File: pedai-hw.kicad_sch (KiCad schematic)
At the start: 31 parts, among them IC1 CD4051BQPWRQ1, IC2 CD4051BQPWRQ1, IC3 CD4051BQPWRQ1, J1 Conn_01x03, J10 Conn_01x01, J11 Conn_01x01, J12 Conn_01x01, J13 Conn_01x01, J14 Conn_01x01, J15 Conn_01x01, J16 left_connector_blackpill, J17 right_connector_blackpill, J18 Conn_01x01, J19 Conn_01x01, J2 Conn_01x01, J20 Conn_01x01, J21 Conn_01x01, J22 Conn_01x01, J23 Conn_01x01, J24 Conn_01x01, J25 Conn_01x01, J26 Conn_01x01, J27 Conn_01x01, J28 Conn_01x01, J3 Conn_01x01, J4 Conn_01x01, J5 Conn_01x01, J6 Conn_01x01, J7 Conn_01x01, J8 Conn_01x01, J9 Conn_01x01

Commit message: board is almost ready for production still looking for mistakes and inaccuracies
Signed-off-by: gmazzucchi <giacomo.mazzucchi@protonmail.com>
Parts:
- added H1, H2: MountingHole, MountingHole:MountingHole_4.3mm_M4, symbol Mechanical:MountingHole
- added J29: Conn_01x01, Connector_Wire:SolderWirePad_1x01_SMD_5x10mm, symbol Connector_Generic:Conn_01x01
- added R1, R2, R3: 1000, Resistor_SMD:R_1206_3216Metric, symbol Device:R
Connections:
- net +3.3V: now also J16.20 (Pin_20), R1.1, R2.1, R3.1; no longer J16.18 (Pin_18)
- net GND: now also J29.1 (Pin_1); no longer J17.2 (Pin_2)
- net MUX_D1: now also R1.2
- net MUX_D2: now also R2.2
- net MUX_D3: now also R3.2
- no-connect marks 27 -> 28
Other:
- note added: "Pull up resistors"

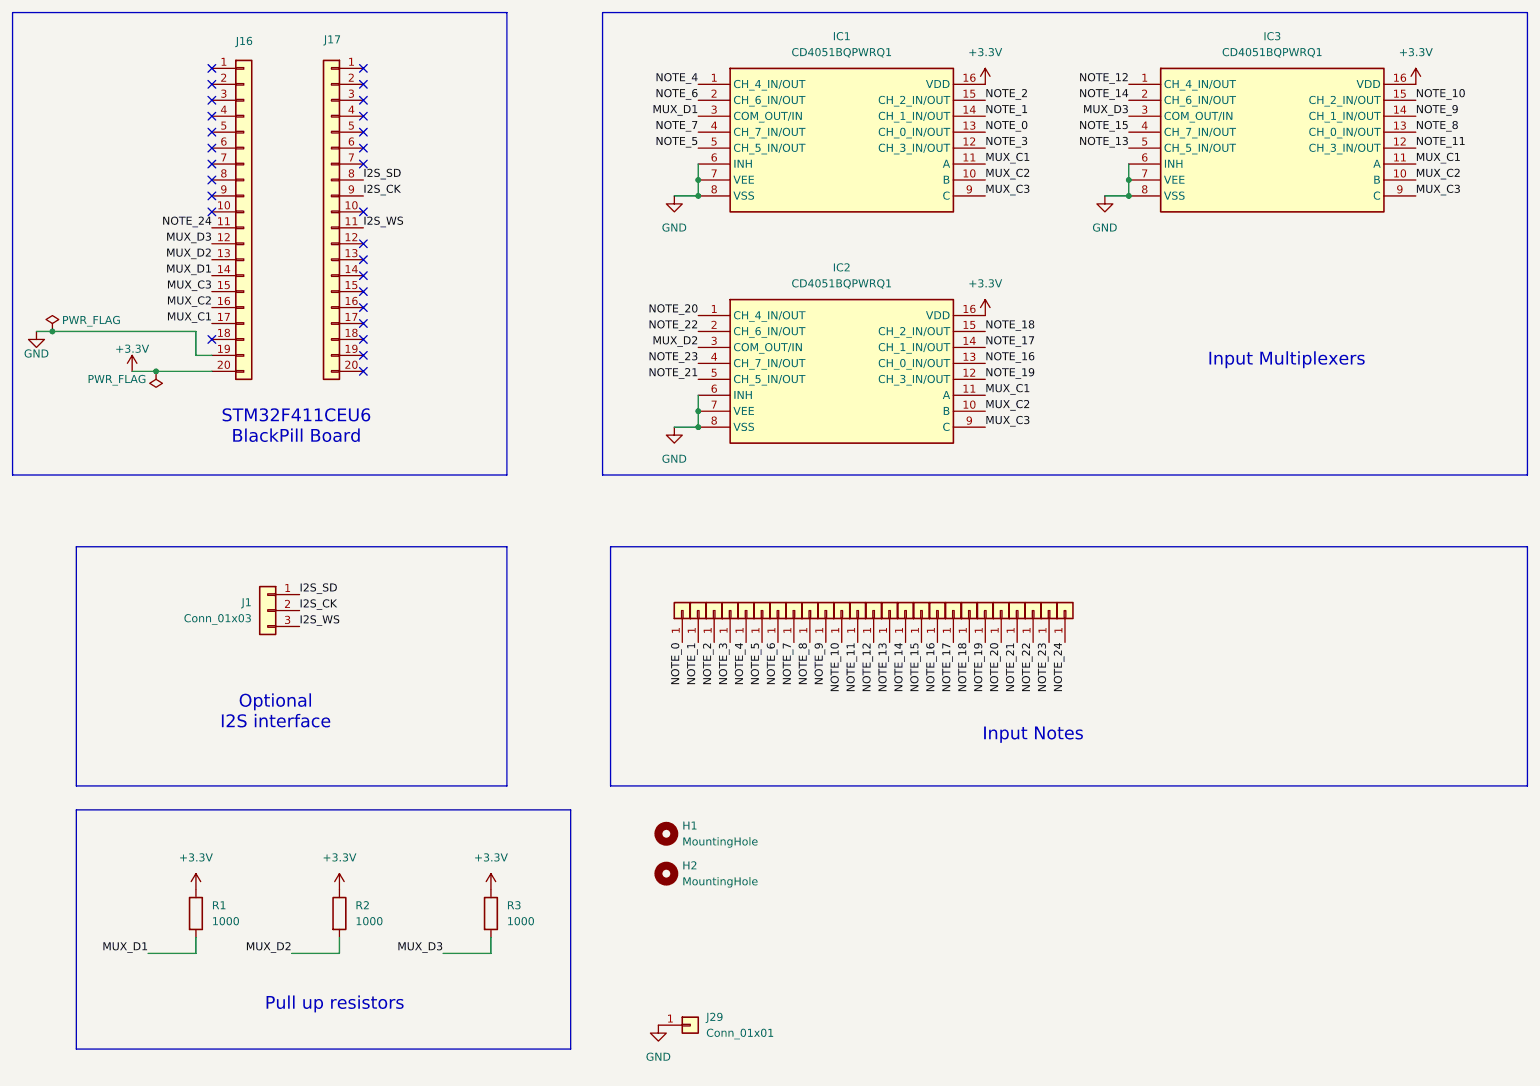
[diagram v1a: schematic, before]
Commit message: fix: removed multiplexer and attached directly to GPIOs fix: removed I2S interface for sound feat: added a UART to communicate with the mainboard
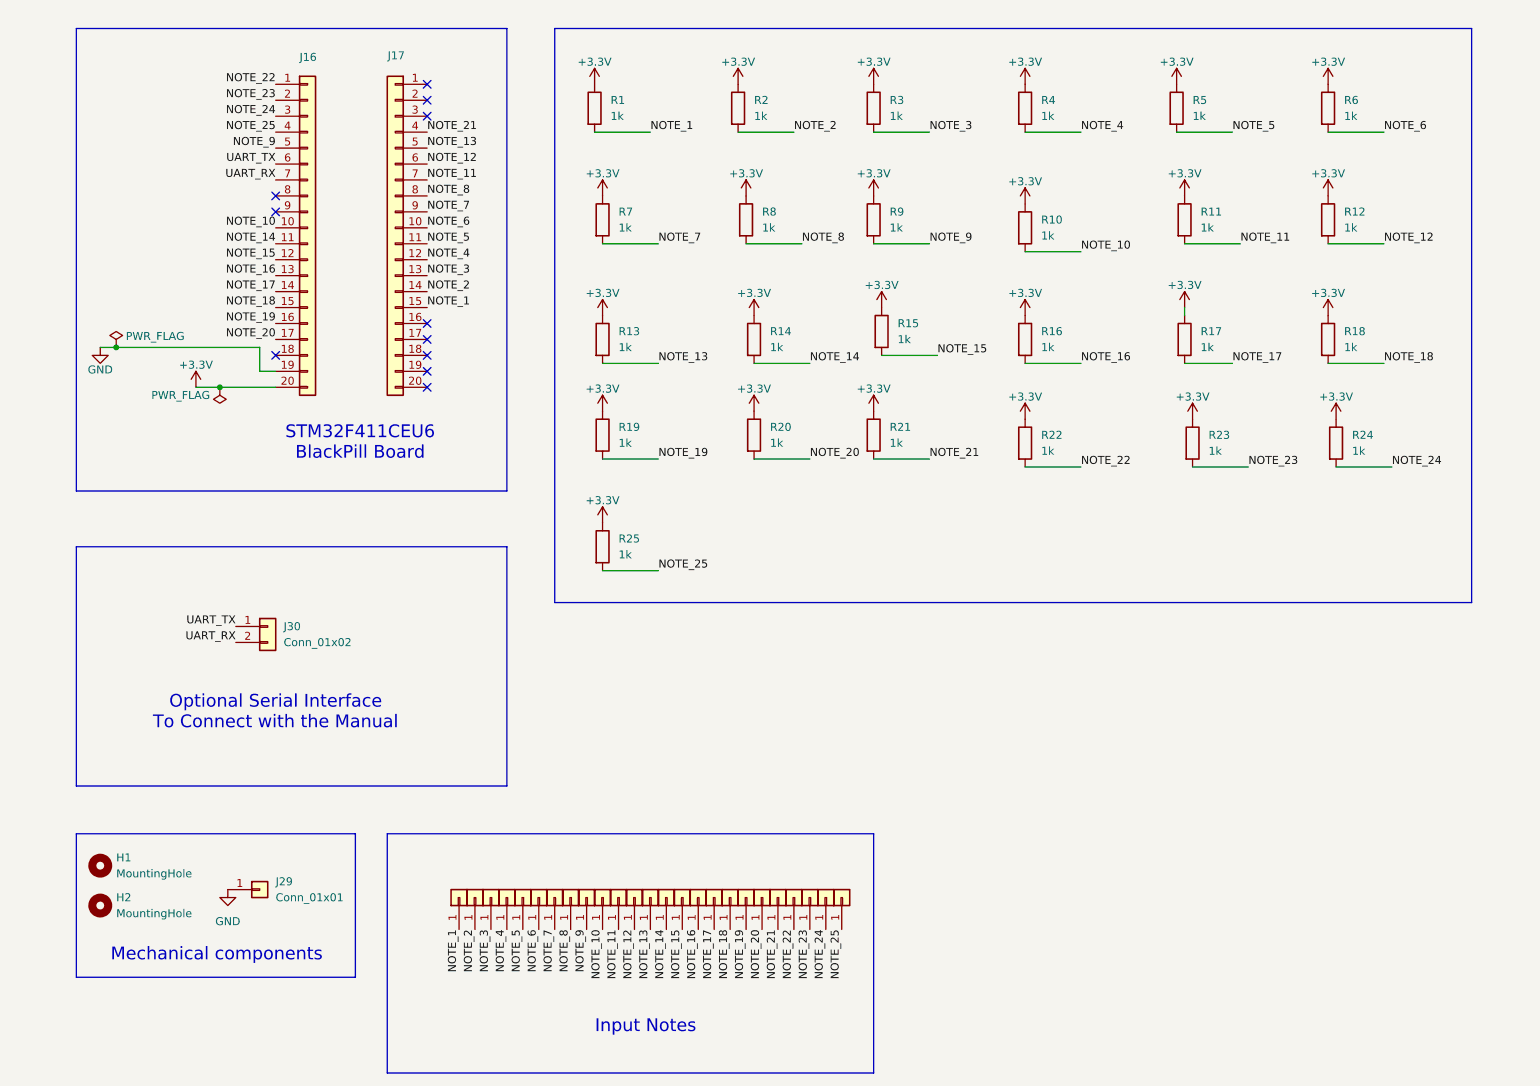
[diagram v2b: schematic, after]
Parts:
- removed IC1, IC2, IC3: CD4051BQPWRQ1, pedalinator_library:CD4051BQ, symbol CD4051BQPWRQ1:CD4051BQPWRQ1
- removed J1: Conn_01x03, Connector_PinHeader_2.00mm:PinHeader_1x03_P2.00mm_Vertical, symbol Connector_Generic:Conn_01x03
- added J30: Conn_01x02, Connector_PinSocket_2.54mm:PinSocket_1x02_P2.54mm_Vertical, symbol Connector_Generic:Conn_01x02
- added R10, R11, R12, R13, R14, R15, R16, R17, R18, R19, R20, R21, R22, R23, R24, R25, R4, R5, R6, R7, R8, R9: 1k, Resistor_THT:R_Axial_DIN0207_L6.3mm_D2.5mm_P10.16mm_Horizontal, symbol Device:R
- R1, R2, R3: value 1000 -> 1k; footprint Resistor_SMD:R_1206_3216Metric -> Resistor_THT:R_Axial_DIN0207_L6.3mm_D2.5mm_P10.16mm_Horizontal
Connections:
- net I2S_CK is gone; now on net NOTE_7: J17.9 (Pin_9)
- net I2S_SD is gone; now on net NOTE_8: J17.8 (Pin_8)
- net I2S_WS is gone; now on net NOTE_5: J17.11 (Pin_11)
- net MUX_C1 is gone; now on net NOTE_20: J16.17 (Pin_17)
- net MUX_C2 is gone; now on net NOTE_19: J16.16 (Pin_16)
- net MUX_C3 is gone; now on net NOTE_18: J16.15 (Pin_15)
- net NOTE_0 is gone; now on net NOTE_1: J2.1 (Pin_1)
- net +3.3V: now also R10.1, R11.1, R12.1, R13.1, R14.1, R15.1, R16.1, R17.1, R18.1, R19.1, R20.1, R21.1, R22.1, R23.1, R24.1, R25.1, R4.1, R5.1, R6.1, R7.1, R8.1, R9.1
- net NOTE_1: now also J17.15 (Pin_15), R1.2; no longer J3.1 (Pin_1)
- net NOTE_10: now also J11.1 (Pin_1), J16.10 (Pin_10), R10.2; no longer J12.1 (Pin_1)
- net NOTE_11: now also J12.1 (Pin_1), J17.7 (Pin_7), R11.2; no longer J13.1 (Pin_1)
- net NOTE_12: now also J13.1 (Pin_1), J17.6 (Pin_6), R12.2; no longer J14.1 (Pin_1)
- net NOTE_13: now also J14.1 (Pin_1), J17.5 (Pin_5), R13.2; no longer J15.1 (Pin_1)
- net NOTE_14: now also J15.1 (Pin_1), J16.11 (Pin_11), R14.2; no longer J18.1 (Pin_1)
- net NOTE_15: now also J16.12 (Pin_12), J18.1 (Pin_1), R15.2; no longer J19.1 (Pin_1)
- net NOTE_16: now also J16.13 (Pin_13), J19.1 (Pin_1), R16.2; no longer J20.1 (Pin_1)
- net NOTE_17: now also J16.14 (Pin_14), J20.1 (Pin_1), R17.2; no longer J21.1 (Pin_1)
- net NOTE_18: now also J21.1 (Pin_1), R18.2; no longer J22.1 (Pin_1)
- net NOTE_19: now also J22.1 (Pin_1), R19.2; no longer J23.1 (Pin_1)
- net NOTE_2: now also J17.14 (Pin_14), J3.1 (Pin_1), R2.2; no longer J4.1 (Pin_1)
- net NOTE_20: now also J23.1 (Pin_1), R20.2; no longer J24.1 (Pin_1)
- net NOTE_21: now also J17.4 (Pin_4), J24.1 (Pin_1), R21.2; no longer J25.1 (Pin_1)
- net NOTE_22: now also J16.1 (Pin_1), J25.1 (Pin_1), R22.2; no longer J26.1 (Pin_1)
- net NOTE_23: now also J16.2 (Pin_2), J26.1 (Pin_1), R23.2; no longer J27.1 (Pin_1)
- net NOTE_24: now also J16.3 (Pin_3), J27.1 (Pin_1), R24.2; no longer J16.11 (Pin_11), J28.1 (Pin_1)
- net NOTE_3: now also J17.13 (Pin_13), J4.1 (Pin_1), R3.2; no longer J5.1 (Pin_1)
- net NOTE_4: now also J17.12 (Pin_12), J5.1 (Pin_1), R4.2; no longer J6.1 (Pin_1)
- net NOTE_5: now also J6.1 (Pin_1), R5.2; no longer J7.1 (Pin_1)
- net NOTE_6: now also J17.10 (Pin_10), J7.1 (Pin_1), R6.2; no longer J8.1 (Pin_1)
- net NOTE_7: now also J8.1 (Pin_1), R7.2; no longer J9.1 (Pin_1)
- net NOTE_8: now also J9.1 (Pin_1), R8.2; no longer J10.1 (Pin_1)
- net NOTE_9: now also J10.1 (Pin_1), J16.5 (Pin_5), R9.2; no longer J11.1 (Pin_1)
- net NOTE_25: now reaches J16.4 (Pin_4)
- net NOTE_25: now also J28.1 (Pin_1), R25.2
- net UART_TX: now reaches J16.6 (Pin_6)
- net UART_TX: now also J30.1 (Pin_1)
- net UART_RX: now reaches J16.7 (Pin_7)
- net UART_RX: now also J30.2 (Pin_2)
- removed net MUX_D1: J16.14 (Pin_14), R1.2
- removed net MUX_D2: J16.13 (Pin_13), R2.2
- removed net MUX_D3: J16.12 (Pin_12), R3.2
- no-connect marks 28 -> 11
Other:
- note added: "Mechanical components"
- note added: "Optional Serial Interface To Connect with the Manual"
- note removed: "Input Multiplexers"
- note removed: "Optional I2S interface"
- note removed: "Pull up resistors"
- moved on the sheet: H1, H2, J16, J17, J29

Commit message: production
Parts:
- added C1: 10u, Capacitor_SMD:C_0603_1608Metric, symbol Device:C
- added C2: 100n, Capacitor_SMD:C_0603_1608Metric, symbol Device:C
- added C3: 220u, Capacitor_SMD:C_0603_1608Metric, symbol Device:C
- added H3, H4, H5: MountingHole, MountingHole:MountingHole_3.2mm_M3_Pad, symbol Mechanical:MountingHole
- H1, H2: footprint MountingHole:MountingHole_4.3mm_M4 -> MountingHole:MountingHole_3.2mm_M3_Pad
- J30: footprint Connector_PinSocket_2.54mm:PinSocket_1x02_P2.54mm_Vertical -> Connector_PinHeader_2.54mm:PinHeader_1x04_P2.54mm_Vertical; symbol Connector_Generic:Conn_01x02 -> Connector_Generic:Conn_01x04
- R1, R10, R11, R12, R13, R14, R15, R16, R17, R18, R19, R2, R20, R21, R22, R23, R24, R25, R3, R4, R5, R6, R7, R8, R9: value 1k -> 4.7k
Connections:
- net +3.3V: now also J30.3 (Pin_3), C1.1, C2.1, C3.1
- net GND: now also J30.4 (Pin_4), C1.2, C2.2, C3.2
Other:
- note added: "Power Flags"
- moved on the sheet: J16, J17
